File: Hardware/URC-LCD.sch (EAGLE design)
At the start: 6 parts, among them IC1 74HC2G125, J1 SPI-LCD

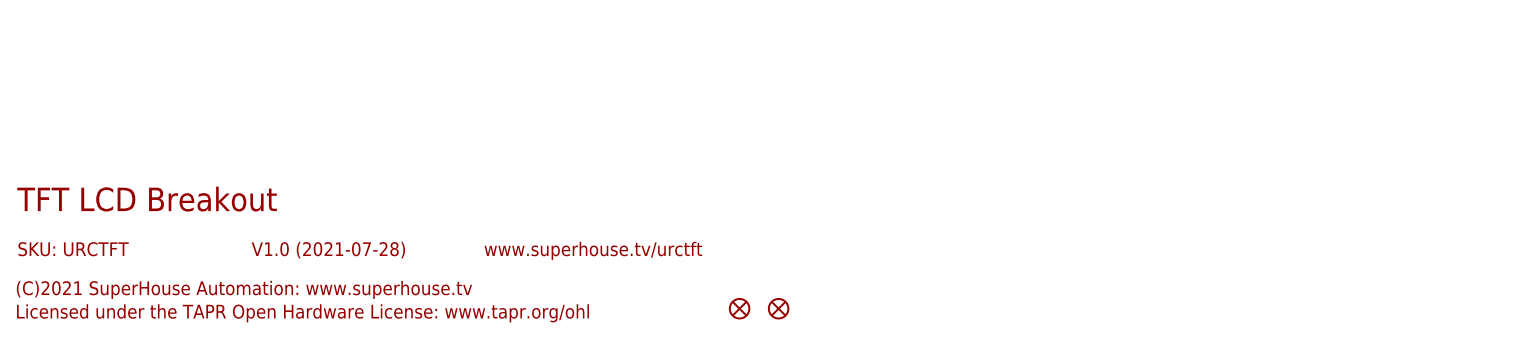
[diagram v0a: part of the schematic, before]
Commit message: Major mechanical shrinkage for revised v1.0 release.
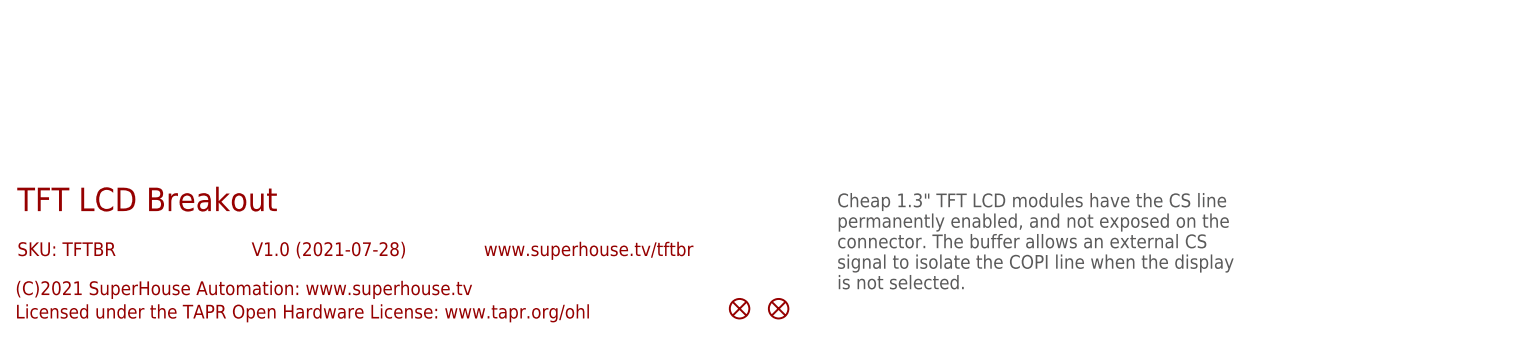
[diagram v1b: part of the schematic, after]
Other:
- note added: "Cheap 1.3" TFT LCD modules have the CS line permanently enabled, and not exposed on the connector. The buffer allows an external CS signal to isolate the COPI line when the display is not selected."
- note added: "SKU: TFTBR"
- note added: "www.superhouse.tv/tftbr"
- note removed: "SKU: URCTFT"
- note removed: "www.superhouse.tv/urctft"
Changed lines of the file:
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@@
 <frame x1="0" y1="0" x2="248.92" y2="185.42" columns="8" rows="5" layer="94"/>
 <text x="7.62" y="20.32" size="3.048" layer="94">TFT LCD Breakout</text>
-<text x="7.62" y="14.478" size="1.778" layer="94">SKU: URCTFT</text>
+<text x="7.62" y="14.478" size="1.778" layer="94">SKU: TFTBR</text>
 <text x="7.366" y="9.398" size="1.778" layer="94">(C)2021 SuperHouse Automation: www.superhouse.tv</text>
 <text x="7.366" y="6.35" size="1.778" layer="94">Licensed under the TAPR Open Hardware License: www.tapr.org/ohl</text>
-<text x="68.326" y="14.478" size="1.778" layer="94">www.superhouse.tv/urctft</text>
+<text x="68.326" y="14.478" size="1.778" layer="94">www.superhouse.tv/tftbr</text>
 <frame x1="5.08" y1="12.7" x2="109.22" y2="25.4" columns="0" rows="0" layer="94" border-left="no" border-top="no" border-right="no" border-bottom="no"/>
 <frame x1="5.08" y1="12.7" x2="35.56" y2="17.78" columns="8" rows="5" layer="94"/>
@@
 <wire x1="157.48" y1="71.12" x2="210.82" y2="71.12" width="0.4064" layer="97" style="longdash"/>
 <text x="162.56" y="139.7" size="2.54" layer="94">LCD Header</text>
+<text x="114.3" y="10.16" size="1.778" layer="97">Cheap 1.3" TFT LCD modules have the CS line
+permanently enabled, and not exposed on the
+connector. The buffer allows an external CS
+signal to isolate the COPI line when the display
+is not selected.</text>
 </plain>
 <instances>
@@
 </drawing>
 <compatibility>
+<note version="6.3" minversion="6.2.2" severity="warning">
+Since Version 6.2.2 text objects can contain more than one line,
+which will not be processed correctly with this version.
+</note>
 <note version="8.2" severity="warning">
 Since Version 8.2, EAGLE supports online libraries. The ids

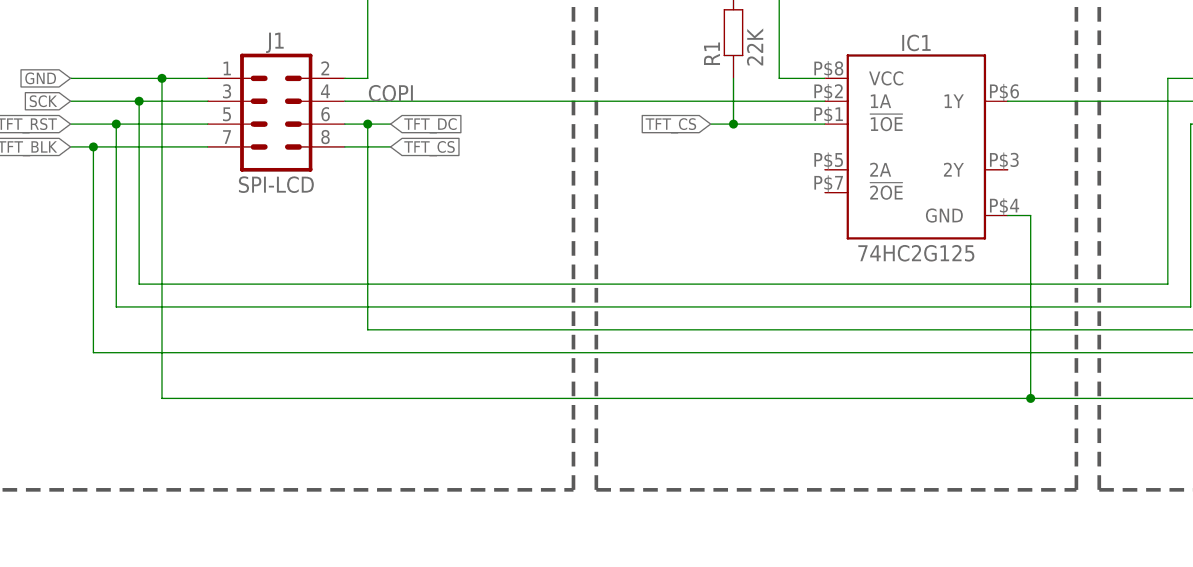
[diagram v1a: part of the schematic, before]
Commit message: Tie unused inputs to GND.
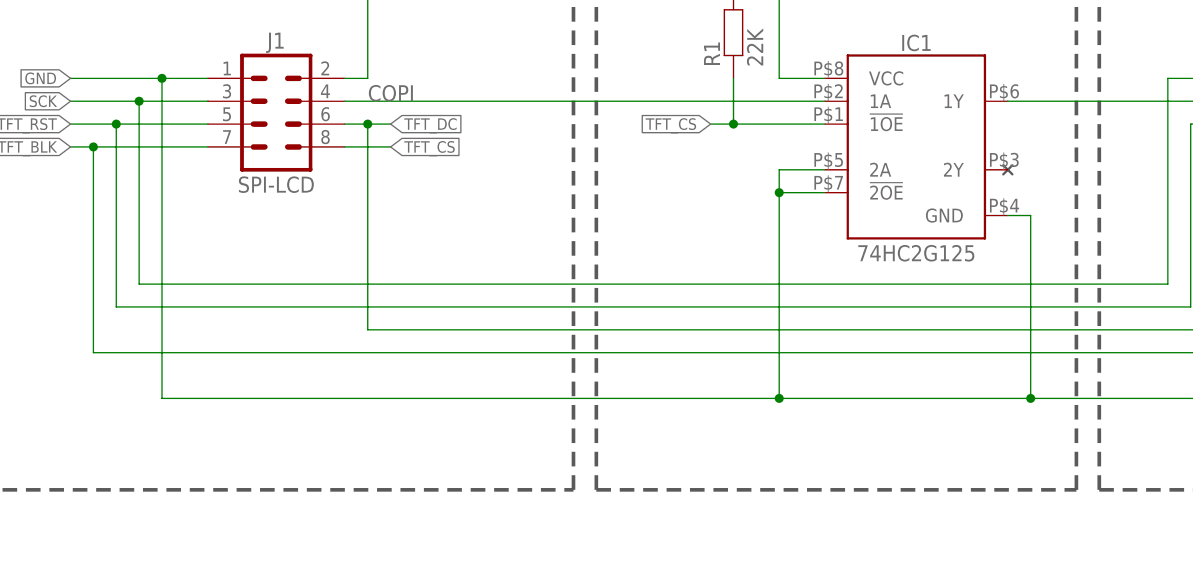
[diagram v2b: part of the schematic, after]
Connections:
- net GND: now also IC1.!2OE, IC1.2A
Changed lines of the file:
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@@
 <part name="IC1" library="SuperHouse-ICs" library_urn="urn:adsk.eagle:library:11768868" deviceset="74HC2G125" device="-TSSOP8" package3d_urn="urn:adsk.eagle:package:23576434/4" value="74HC2G125"/>
 <part name="R1" library="SuperHouse-Resistors" library_urn="urn:adsk.eagle:library:28961094" deviceset="RESISTOR" device="0603" package3d_urn="urn:adsk.eagle:package:28961141/1" value="22K"/>
+<part name="NC1" library="SuperHouse-SupplySymbols" library_urn="urn:adsk.eagle:library:11790503" deviceset="NC" device=""/>
 </parts>
 <sheets>
@@
 <attribute name="VALUE" x="120.142" y="118.11" size="1.778" layer="96" rot="R90"/>
 </instance>
+<instance part="NC1" gate="G$1" x="147.32" y="106.68" smashed="yes"/>
 </instances>
 <busses>
@@
 <wire x1="58.42" y1="116.84" x2="53.34" y2="116.84" width="0.1524" layer="91"/>
 <wire x1="53.34" y1="116.84" x2="53.34" y2="81.28" width="0.1524" layer="91"/>
-<wire x1="53.34" y1="81.28" x2="149.86" y2="81.28" width="0.1524" layer="91"/>
+<wire x1="53.34" y1="81.28" x2="121.92" y2="81.28" width="0.1524" layer="91"/>
 <junction x="149.86" y="81.28"/>
+<wire x1="121.92" y1="81.28" x2="149.86" y2="81.28" width="0.1524" layer="91"/>
 <wire x1="53.34" y1="116.84" x2="43.18" y2="116.84" width="0.1524" layer="91"/>
 <junction x="53.34" y="116.84"/>
 <label x="43.18" y="116.84" size="1.27" layer="95" rot="R180" xref="yes"/>
+<pinref part="IC1" gate="G$1" pin="2A"/>
+<wire x1="127" y1="106.68" x2="121.92" y2="106.68" width="0.1524" layer="91"/>
+<wire x1="121.92" y1="106.68" x2="121.92" y2="104.14" width="0.1524" layer="91"/>
+<junction x="121.92" y="81.28"/>
+<pinref part="IC1" gate="G$1" pin="!2OE"/>
+<wire x1="121.92" y1="104.14" x2="121.92" y2="81.28" width="0.1524" layer="91"/>
+<wire x1="127" y1="104.14" x2="121.92" y2="104.14" width="0.1524" layer="91"/>
+<junction x="121.92" y="104.14"/>
 </segment>
 </net>
